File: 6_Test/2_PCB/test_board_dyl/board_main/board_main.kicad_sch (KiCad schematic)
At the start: 1 part

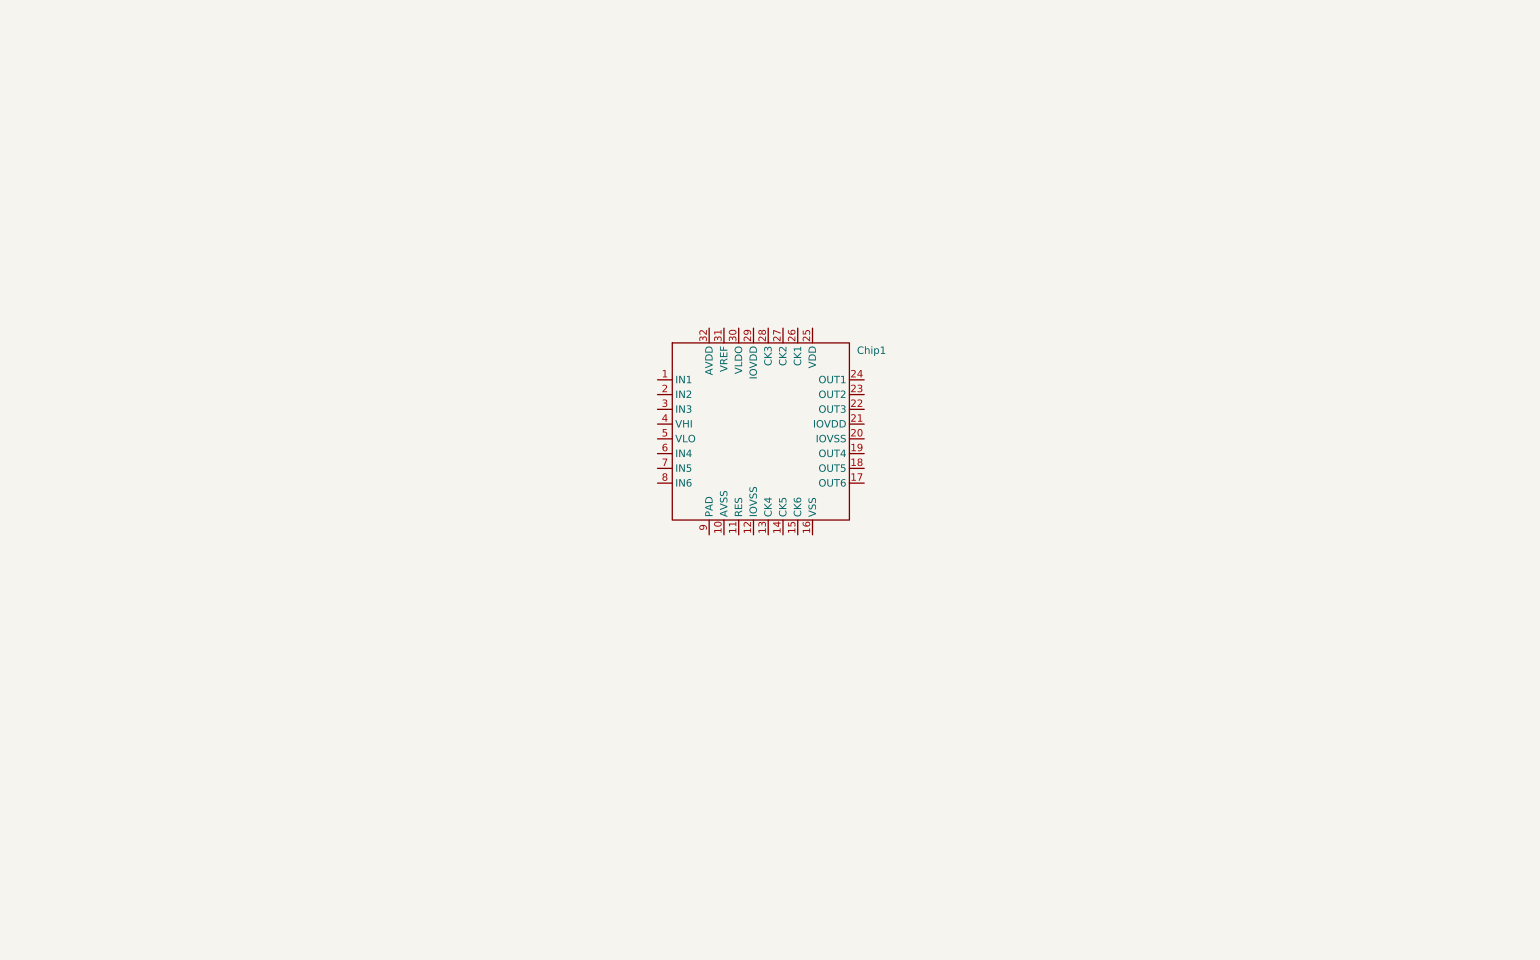
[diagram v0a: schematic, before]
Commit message: Updated board schematic
Integrating the power supplies on separate sheets. Includes the ADC chip and socket and connecting circuitry.
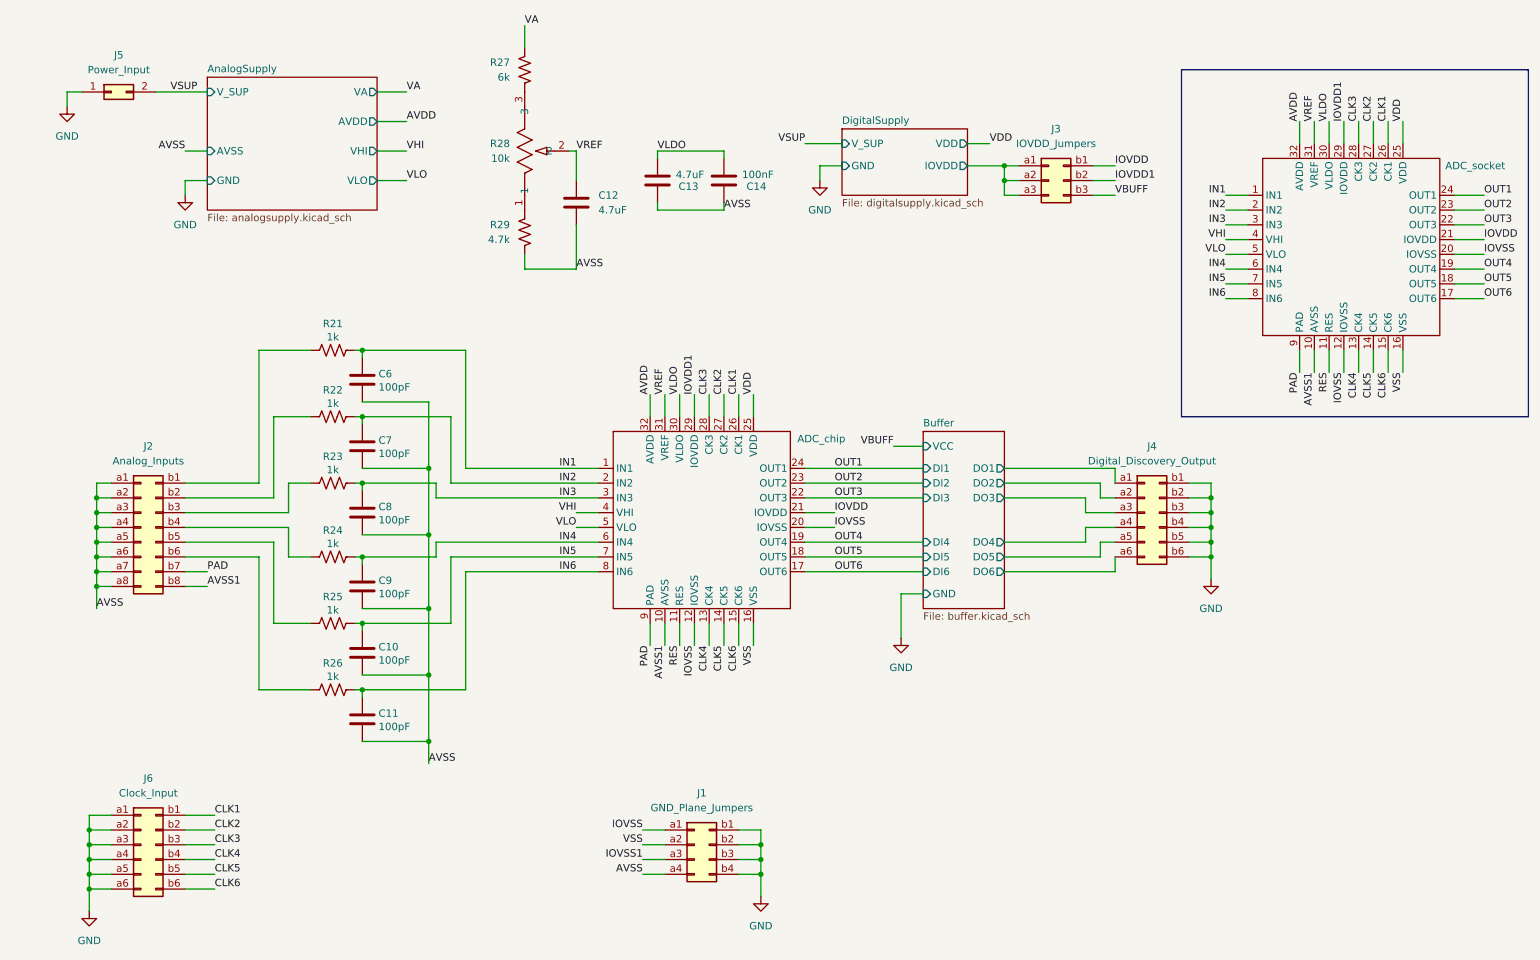
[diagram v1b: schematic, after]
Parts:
- added ADC_socket: ~, Package_DIP:DIP-32_W15.24mm_Socket, symbol chip:Chip
- added C10, C11, C6, C7, C8, C9: 100pF, symbol Device:C
- added C12, C13: 4.7uF, symbol Device:C
- added C14: 100nF, symbol Device:C
- added J1: GND_Plane_Jumpers, Connector_PinHeader_2.54mm:PinHeader_2x04_P2.54mm_Vertical, symbol Connector_Generic:Conn_02x04_Row_Letter_First
- added J2: Analog_Inputs, symbol Connector_Generic:Conn_02x08_Row_Letter_First
- added J3: IOVDD_Jumpers, symbol Connector_Generic:Conn_02x03_Row_Letter_First
- added J4: Digital_Discovery_Output, symbol Connector_Generic:Conn_02x06_Row_Letter_First
- added J5: Power_Input, symbol Connector_Generic:Conn_02x01
- added J6: Clock_Input, symbol Connector_Generic:Conn_02x06_Row_Letter_First
- added R21, R22, R23, R24, R25, R26: 1k, symbol Device:R_US
- added R27: 6k, symbol Device:R_US
- added R28: 10k, POT_PV37W_MUR, symbol pot10turn:PV37W103C01B00
- added R29: 4.7k, symbol Device:R_US
- renumbered Chip1 to ADC_chip
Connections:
- net IN1: now reaches ADC_chip.1 (IN1)
- net IN1: now also ADC_socket.1 (IN1), C6.1, R21.2
- net AVSS1: now reaches ADC_chip.10 (AVSS)
- net AVSS1: now also ADC_socket.10 (AVSS), J2.b8 (Pin_b8)
- net RES: now reaches ADC_chip.11 (RES)
- net RES: now also ADC_socket.11 (RES)
- net IOVSS: now reaches ADC_chip.12 (IOVSS)
- net IOVSS: now also ADC_chip.20 (IOVSS), ADC_socket.12 (IOVSS), ADC_socket.20 (IOVSS), J1.a1 (Pin_a1)
- net CLK4: now reaches ADC_chip.13 (CK4)
- net CLK4: now also ADC_socket.13 (CK4), J6.b4 (Pin_b4)
- net CLK5: now reaches ADC_chip.14 (CK5)
- net CLK5: now also ADC_socket.14 (CK5), J6.b5 (Pin_b5)
- net CLK6: now reaches ADC_chip.15 (CK6)
- net CLK6: now also ADC_socket.15 (CK6), J6.b6 (Pin_b6)
- net VSS: now reaches ADC_chip.16 (VSS)
- net VSS: now also ADC_socket.16 (VSS), J1.a2 (Pin_a2)
- net OUT6: now reaches ADC_chip.17 (OUT6)
- net OUT6: now also ADC_socket.17 (OUT6)
- net OUT5: now reaches ADC_chip.18 (OUT5)
- net OUT5: now also ADC_socket.18 (OUT5)
- net OUT4: now reaches ADC_chip.19 (OUT4)
- net OUT4: now also ADC_socket.19 (OUT4)
- net IN2: now reaches ADC_chip.2 (IN2)
- net IN2: now also ADC_socket.2 (IN2), C7.1, R22.2
- net IOVDD: now reaches ADC_chip.21 (IOVDD)
- net IOVDD: now also ADC_socket.21 (IOVDD), J3.b1 (Pin_b1)
- net OUT3: now reaches ADC_chip.22 (OUT3)
- net OUT3: now also ADC_socket.22 (OUT3)
- net OUT2: now reaches ADC_chip.23 (OUT2)
- net OUT2: now also ADC_socket.23 (OUT2)
- net OUT1: now reaches ADC_chip.24 (OUT1)
- net OUT1: now also ADC_socket.24 (OUT1)
- net VDD: now reaches ADC_chip.25 (VDD)
- net VDD: now also ADC_socket.25 (VDD)
- net CLK1: now reaches ADC_chip.26 (CK1)
- net CLK1: now also ADC_socket.26 (CK1), J6.b1 (Pin_b1)
- net CLK2: now reaches ADC_chip.27 (CK2)
- net CLK2: now also ADC_socket.27 (CK2), J6.b2 (Pin_b2)
- net CLK3: now reaches ADC_chip.28 (CK3)
- net CLK3: now also ADC_socket.28 (CK3), J6.b3 (Pin_b3)
- net IOVDD1: now reaches ADC_chip.29 (IOVDD)
- net IOVDD1: now also ADC_socket.29 (IOVDD), J3.b2 (Pin_b2)
- net IN3: now reaches ADC_chip.3 (IN3)
- net IN3: now also ADC_socket.3 (IN3), C8.1, R23.2
- net VLDO: now reaches ADC_chip.30 (VLDO)
- net VLDO: now also ADC_socket.30 (VLDO), C13.1, C14.1
- net VREF: now reaches ADC_chip.31 (VREF)
- net VREF: now also ADC_socket.31 (VREF), C12.1, R28.2
- net AVDD: now reaches ADC_chip.32 (AVDD)
- net AVDD: now also ADC_socket.32 (AVDD)
- net VHI: now reaches ADC_chip.4 (VHI)
- net VHI: now also ADC_socket.4 (VHI)
- net VLO: now reaches ADC_chip.5 (VLO)
- net VLO: now also ADC_socket.5 (VLO)
- net IN4: now reaches ADC_chip.6 (IN4)
- net IN4: now also ADC_socket.6 (IN4), C9.1, R24.2
- net IN5: now reaches ADC_chip.7 (IN5)
- net IN5: now also ADC_socket.7 (IN5), C10.1, R25.2
- net IN6: now reaches ADC_chip.8 (IN6)
- net IN6: now also ADC_socket.8 (IN6), C11.1, R26.2
- net PAD: now reaches ADC_chip.9 (PAD)
- net PAD: now also ADC_socket.9 (PAD), J2.b7 (Pin_b7)
- new net: R27.2, R28.3
- new net: J2.b4 (Pin_b4), R24.1
- new net: R28.1, R29.1
- new net: J2.b5 (Pin_b5), R25.1
- new net: J2.b3 (Pin_b3), R23.1
- new net: J2.b1 (Pin_b1), R21.1
- new net: J2.b2 (Pin_b2), R22.1
- new net: J2.b6 (Pin_b6), R26.1
- new net AVSS: C10.2, C11.2, C12.2, C13.2, C14.2, C6.2, C7.2, C8.2, C9.2, J1.a4 (Pin_a4), J2.a1 (Pin_a1), J2.a2 (Pin_a2), J2.a3 (Pin_a3), J2.a4 (Pin_a4), J2.a5 (Pin_a5), J2.a6 (Pin_a6), J2.a7 (Pin_a7), J2.a8 (Pin_a8), R29.2
- new net Buffer/DO1: J4.a1 (Pin_a1)
- new net Buffer/DO2: J4.a2 (Pin_a2)
- new net Buffer/DO3: J4.a3 (Pin_a3)
- new net Buffer/DO4: J4.a4 (Pin_a4)
- new net Buffer/DO5: J4.a5 (Pin_a5)
- new net Buffer/DO6: J4.a6 (Pin_a6)
- new net DigitalSupply/IOVDD: J3.a1 (Pin_a1), J3.a2 (Pin_a2), J3.a3 (Pin_a3)
- new net GND: J1.b1 (Pin_b1), J1.b2 (Pin_b2), J1.b3 (Pin_b3), J1.b4 (Pin_b4), J4.b1 (Pin_b1), J4.b2 (Pin_b2), J4.b3 (Pin_b3), J4.b4 (Pin_b4), J4.b5 (Pin_b5), J4.b6 (Pin_b6), J5.1 (Pin_1), J6.a1 (Pin_a1), J6.a2 (Pin_a2), J6.a3 (Pin_a3), J6.a4 (Pin_a4), J6.a5 (Pin_a5), J6.a6 (Pin_a6)
- new net IOVSS1: J1.a3 (Pin_a3)
- new net VA: R27.1
- new net VBUFF: J3.b3 (Pin_b3)
- new net VSUP: J5.2 (Pin_2)
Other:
- added sheet AnalogSupply (analogsupply.kicad_sch)
- added sheet Buffer (buffer.kicad_sch)
- added sheet DigitalSupply (digitalsupply.kicad_sch)
- moved on the sheet: ADC_chip

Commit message: Fixed comments
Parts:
- removed J1: GND_Plane_Jumpers, Connector_PinHeader_2.54mm:PinHeader_2x04_P2.54mm_Vertical, symbol Connector_Generic:Conn_02x04_Row_Letter_First
- removed J2: Analog_Inputs, symbol Connector_Generic:Conn_02x08_Row_Letter_First
- removed J3: IOVDD_Jumpers, symbol Connector_Generic:Conn_02x03_Row_Letter_First
- removed J4: Digital_Discovery_Output, symbol Connector_Generic:Conn_02x06_Row_Letter_First
- removed J5: Power_Input, symbol Connector_Generic:Conn_02x01
- removed J6: Clock_Input, symbol Connector_Generic:Conn_02x06_Row_Letter_First
- added J1: Digital_Outputs, symbol Connector_Generic:Conn_01x06
- added J10: Analog_Inputs_Jumpers, symbol Connector_Generic:Conn_02x06_Row_Letter_First
- added J3: BNC1, CONN_1274571-1_TYCO, symbol bnc_mini:1274571-1
- added J4: Digital_Inputs, symbol Connector_Generic:Conn_01x08
- added J5: BNC_to_Analog, symbol Connector_Generic:Conn_02x06_Row_Letter_First
- added J6: BNC2, CONN_1274571-1_TYCO, symbol bnc_mini:1274571-1
- added J7: Conn_02x06_Row_Letter_First, symbol Connector_Generic:Conn_02x06_Row_Letter_First
- added J8: IOVDD_Jumpers, symbol Connector_Generic:Conn_02x04_Row_Letter_First
- added J9: Power_Connector, symbol Connector_Generic:Conn_01x02
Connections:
- net AVSS: now also J10.a1 (Pin_a1), J10.a2 (Pin_a2), J10.a3 (Pin_a3), J10.a4 (Pin_a4), J10.a5 (Pin_a5), J10.a6 (Pin_a6), J7.a1 (Pin_a1)
- net AVSS1: now also J7.a5 (Pin_a5)
- net Buffer/DO1: now also J1.1 (Pin_1)
- net Buffer/DO2: now also J1.2 (Pin_2)
- net Buffer/DO3: now also J1.3 (Pin_3)
- net Buffer/DO4: now also J1.4 (Pin_4)
- net Buffer/DO5: now also J1.5 (Pin_5)
- net Buffer/DO6: now also J1.6 (Pin_6)
- net DigitalSupply/IOVDD: now also J8.a2 (Pin_a2), J8.a3 (Pin_a3), J8.a4 (Pin_a4)
- net GND: now also J4.8 (Pin_8), J7.b1 (Pin_b1), J7.b2 (Pin_b2), J7.b3 (Pin_b3), J7.b4 (Pin_b4), J7.b5 (Pin_b5), J7.b6 (Pin_b6), J9.2 (Pin_2)
- net IOVDD: now also J8.b2 (Pin_b2)
- net IOVDD1: now also J8.b3 (Pin_b3)
- net IOVSS: now also J7.a2 (Pin_a2)
- net IOVSS1: now also J7.a4 (Pin_a4)
- net PAD: now also J7.a6 (Pin_a6)
- net VBUFF: now also J8.b4 (Pin_b4)
- net VDD: now also J8.b1 (Pin_b1)
- net VSS: now also J7.a3 (Pin_a3)
- net VSUP: now also J9.1 (Pin_1)
- net at R24.1: now also J10.b4 (Pin_b4), J5.b4 (Pin_b4)
- net at R25.1: now also J10.b5 (Pin_b5), J5.b5 (Pin_b5)
- net at R23.1: now also J10.b3 (Pin_b3), J5.b3 (Pin_b3)
- net at R21.1: now also J10.b1 (Pin_b1), J5.b1 (Pin_b1)
- net at R22.1: now also J10.b2 (Pin_b2), J5.b2 (Pin_b2)
- net at R26.1: now also J10.b6 (Pin_b6), J5.b6 (Pin_b6)
- new net: J5.a2 (Pin_a2), J5.a4 (Pin_a4), J5.a6 (Pin_a6), J6.1
- new net: J3.1, J5.a1 (Pin_a1), J5.a3 (Pin_a3), J5.a5 (Pin_a5)
- new net CLK_IN1: J4.2 (Pin_2)
- new net CLK_IN2: J4.3 (Pin_3)
- new net CLK_IN3: J4.4 (Pin_4)
- new net CLK_IN4: J4.5 (Pin_5)
- new net CLK_IN5: J4.6 (Pin_6)
- new net CLK_IN6: J4.7 (Pin_7)
- new net DigitalSupply/VDD: J8.a1 (Pin_a1)
- new net RES_IN: J4.1 (Pin_1)
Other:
- sheet Buffer ports: added CLK1, CLK2, CLK4, CLK5, CLK6, CLK_IN1, CLK_IN2, CLK_IN3, CLK_IN4, CLK_IN5, CLK_IN6, CLk3, RES, RES_IN; removed none
- moved on the sheet: C10, C11, C6, C7, C8, C9, R21, R22, R23, R24, R25, R26

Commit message: final draft of board done.
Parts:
- J10: footprint (none) -> Connector_PinHeader_1.00mm:PinHeader_1x15_P1.00mm_Vertical
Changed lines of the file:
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@@
 			)
 		)
-		(property "Footprint" ""
+		(property "Footprint" "Connector_PinHeader_1.00mm:PinHeader_1x15_P1.00mm_Vertical"
 			(at 44.45 135.89 0)
 			(effects
